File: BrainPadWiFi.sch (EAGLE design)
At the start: 14 parts, among them IC1 ESP-WROOM-02FRONT-FACE, U1 LM3940IMP-3.3/NOPBMP04A-M

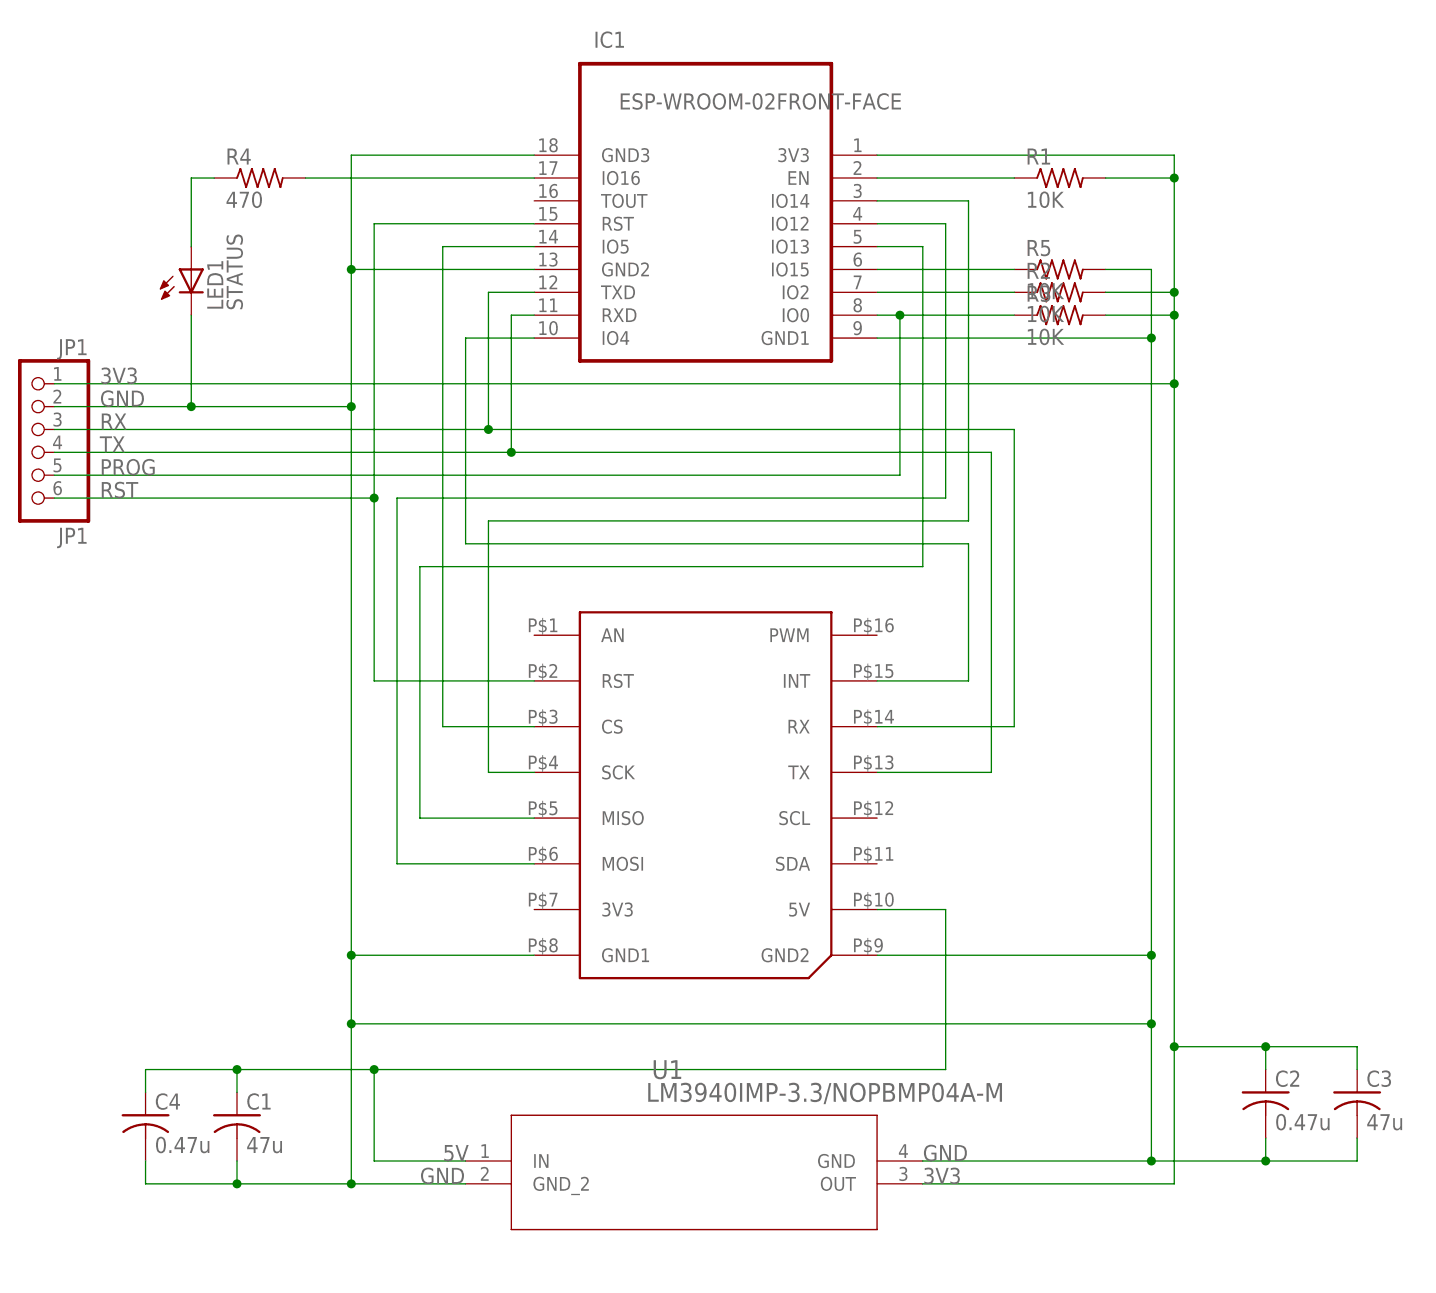
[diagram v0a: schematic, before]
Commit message: Changed regulator.
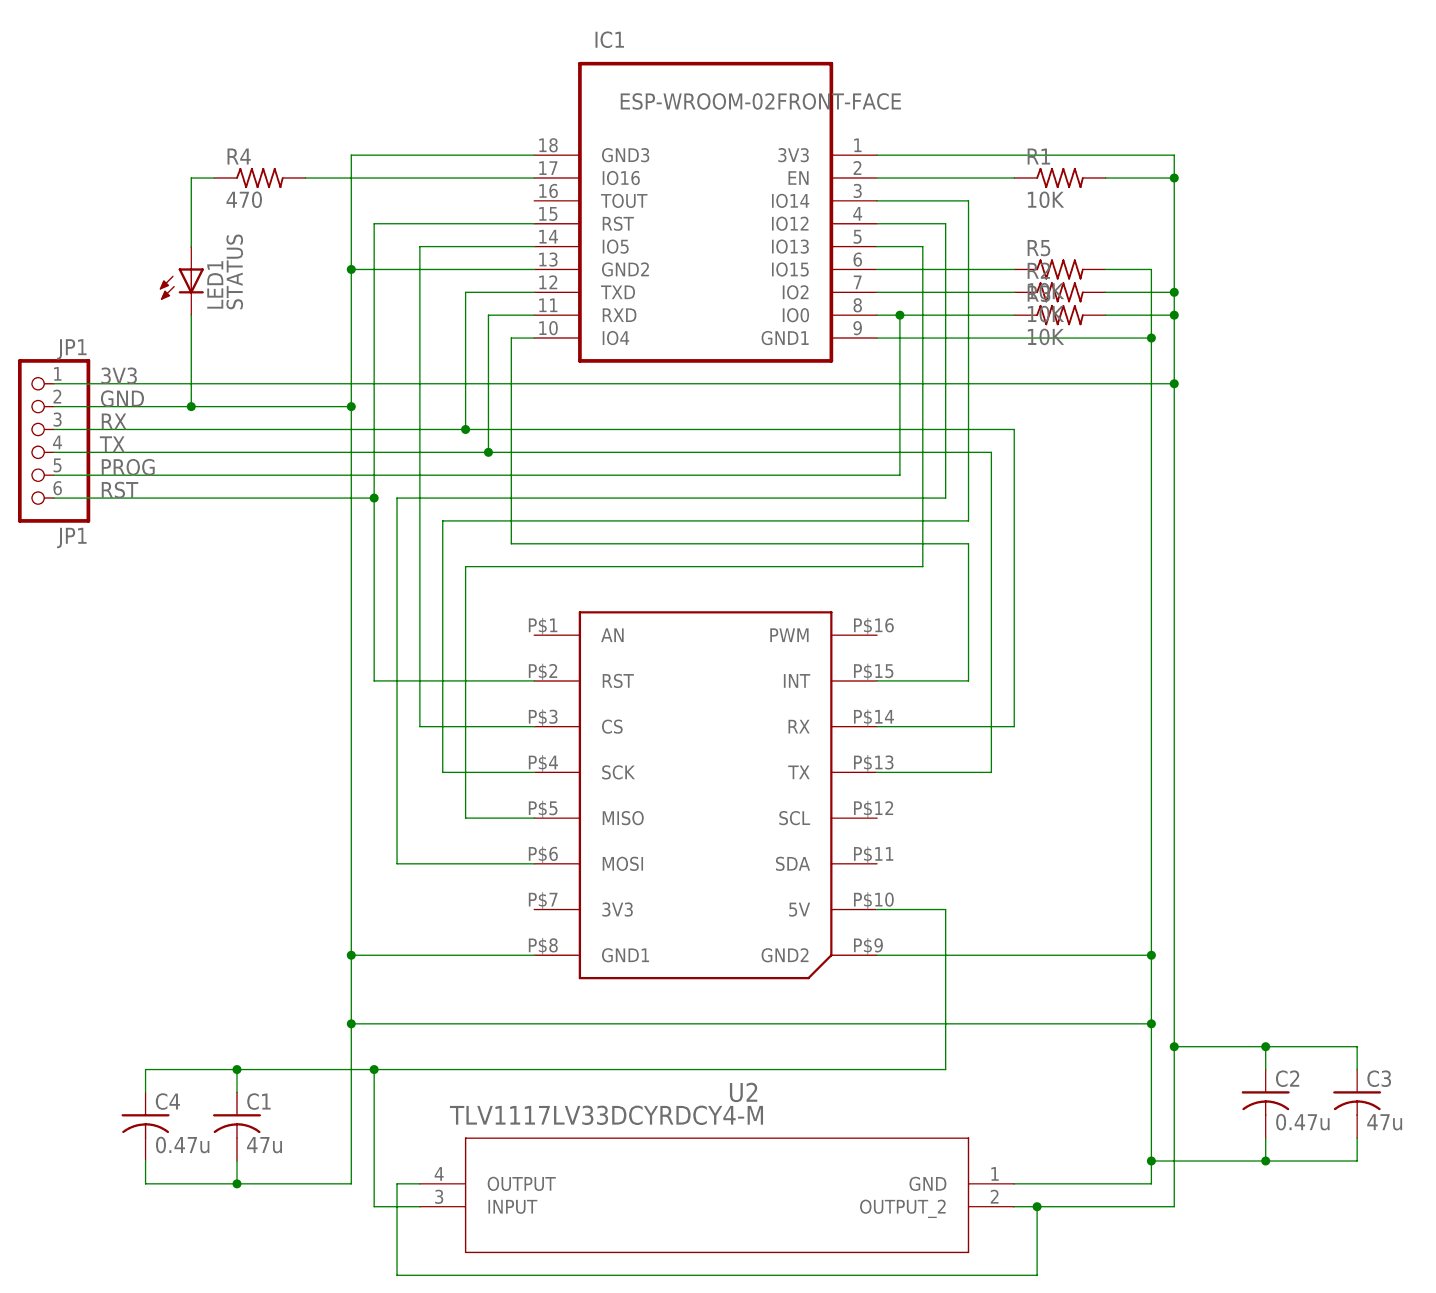
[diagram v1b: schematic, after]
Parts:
- removed U1: LM3940IMP-3.3/NOPBMP04A-M, BrainPadWiFi:LM3940IMP-3.3/NOPBMP04A-M
- added U2: TLV1117LV33DCYRDCY4-M, BrainPadWiFi:TLV1117LV33DCYRDCY4-M
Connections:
- net 3V3: now also U2.OUTPUT, U2.OUTPUT_2; no longer U1.OUT
- net 5V: now also U2.INPUT; no longer U1.IN
- net GND: now also U2.GND; no longer U1.GND, U1.GND_2

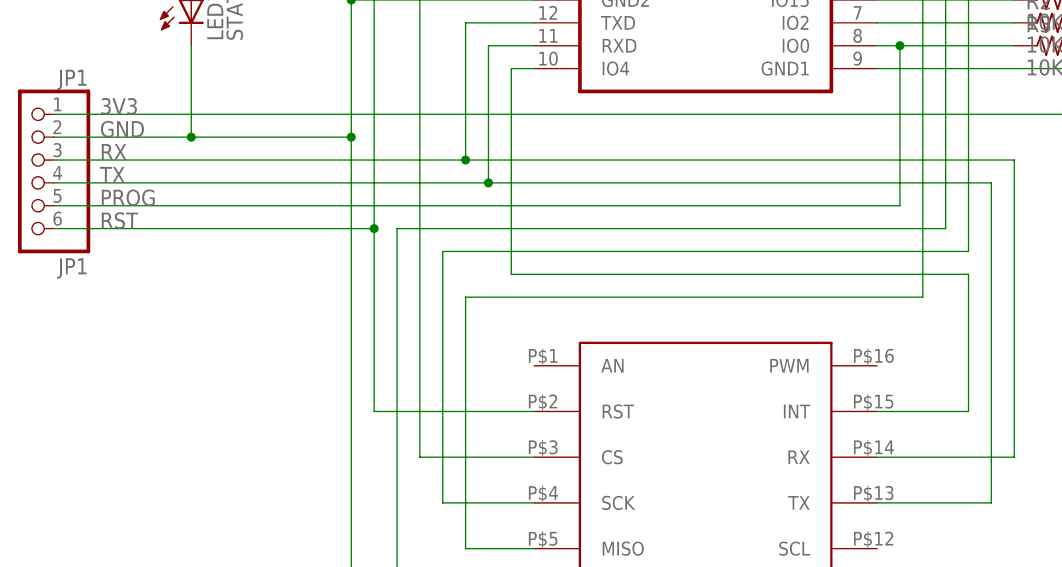
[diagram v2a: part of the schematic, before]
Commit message: PROG line wired because we grant to an ability for self-programming from BrainPad to ESP.
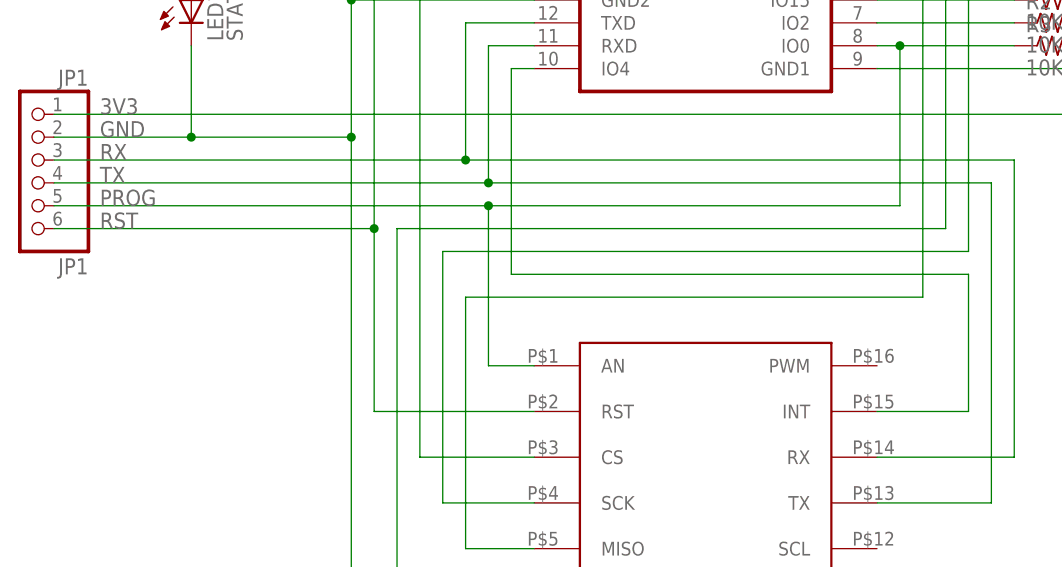
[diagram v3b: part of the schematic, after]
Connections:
- net PROG: now also U$1.AN
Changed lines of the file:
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@@
 <?xml version="1.0" encoding="utf-8"?>
 <!DOCTYPE eagle SYSTEM "eagle.dtd">
-<eagle version="8.7.1">
+<eagle version="9.1.3">
 <drawing>
 <settings>
-<setting alwaysvectorfont="no"/>
+<setting alwaysvectorfont="yes"/>
 <setting verticaltext="up"/>
 </settings>
@@
 <wire x1="101.6" y1="106.68" x2="104.14" y2="106.68" width="0.1524" layer="91"/>
 <wire x1="104.14" y1="106.68" x2="104.14" y2="88.9" width="0.1524" layer="91"/>
-<wire x1="104.14" y1="88.9" x2="10.16" y2="88.9" width="0.1524" layer="91"/>
+<wire x1="104.14" y1="88.9" x2="58.42" y2="88.9" width="0.1524" layer="91"/>
 <pinref part="R3" gate="G$1" pin="1"/>
+<wire x1="58.42" y1="88.9" x2="10.16" y2="88.9" width="0.1524" layer="91"/>
 <wire x1="104.14" y1="106.68" x2="116.84" y2="106.68" width="0.1524" layer="91"/>
 <junction x="104.14" y="106.68"/>
 <label x="15.24" y="88.9" size="1.778" layer="95"/>
 <pinref part="JP1" gate="A" pin="5"/>
-</segment>
-</net>
+<pinref part="U$1" gate="G$1" pin="AN"/>
+<wire x1="58.42" y1="88.9" x2="58.42" y2="71.12" width="0.1524" layer="91"/>
+<wire x1="58.42" y1="71.12" x2="63.5" y2="71.12" width="0.1524" layer="91"/>
+<junction x="58.42" y="88.9"/>
+</segment>
+</net>

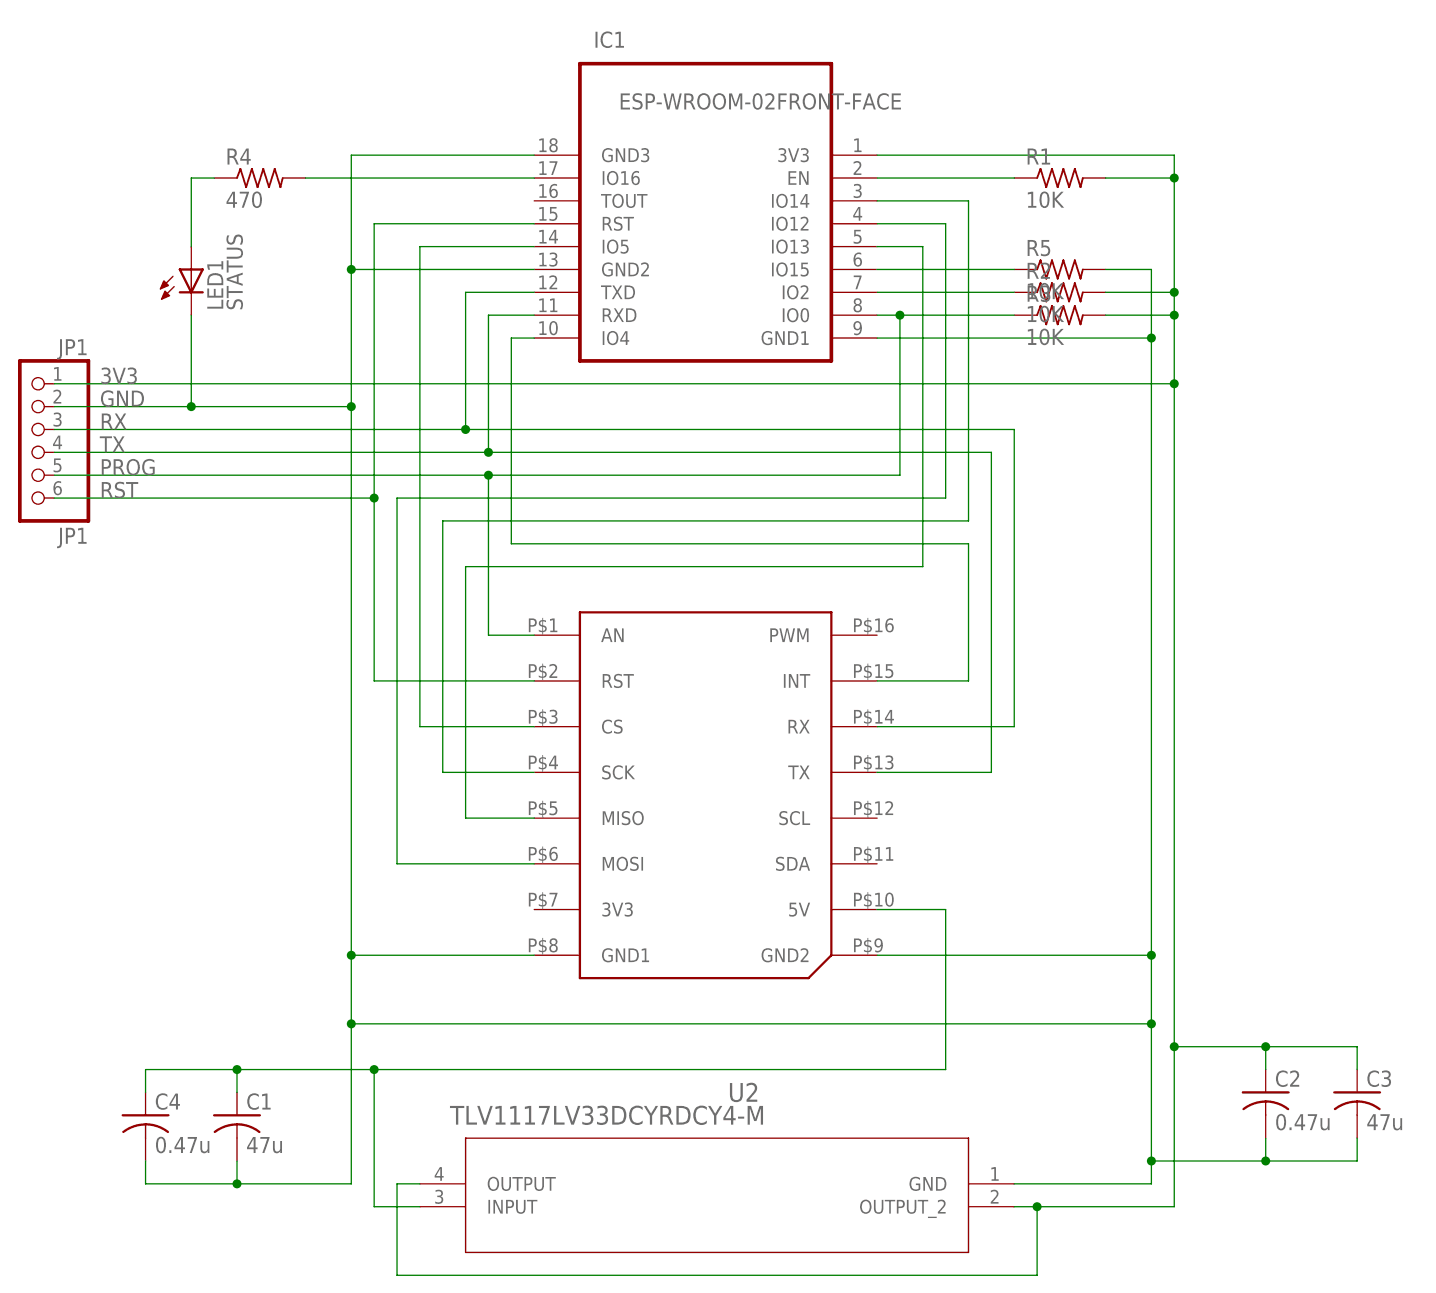
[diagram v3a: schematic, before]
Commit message: Redesigned for next version.
SMT pieces place only front side. (exclude ESP)
Add grove connector.
Registers only 1K.
Add status2 LED.
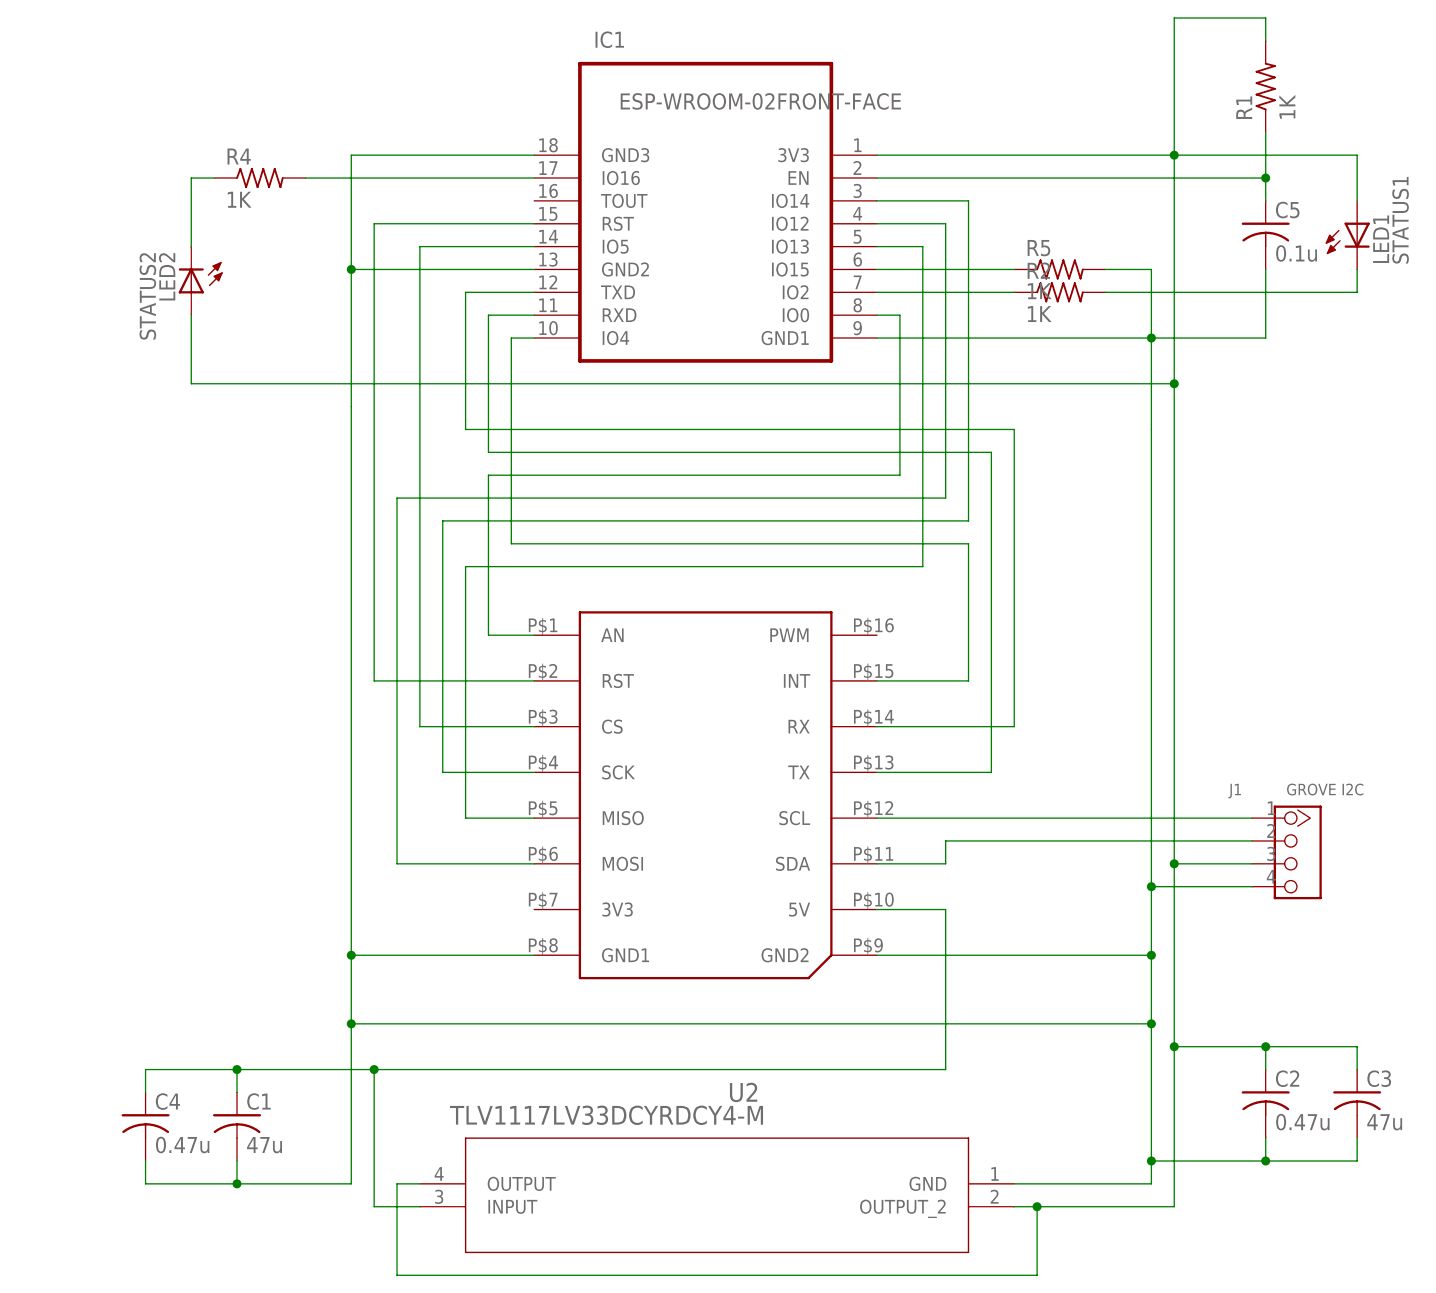
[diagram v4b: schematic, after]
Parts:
- removed JP1: JP1, BrainPadWiFi:PINHD-1X6
- removed R3: 10K, BrainPadWiFi:R-US_R1206
- added C5: 0.1u, BrainPadWiFi:C-USC1206
- added J1: GROVE I2C, BrainPadWiFi:GROVE-CONNECTOR-DIP(4P-2.0)
- added LED2: STATUS2, BrainPadWiFi:LEDSML1206
- LED1: value STATUS -> STATUS1
- R1, R2, R5: value 10K -> 1K
- R4: value 470 -> 1K
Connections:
- net N$1 renamed IO2
- net N$4 renamed IO15
- removed net STAT: LED1.A, R4.1
- new net SCL: J1.1, U$1.SCL
- new net SDA: J1.2, U$1.SDA
- new net STAT1: LED1.C, R2.2
- new net STAT2: LED2.C, R4.1
- net 3V3: now also J1.3, LED1.A, LED2.A; no longer JP1.1, R2.2, R3.2
- net EN: now also C5.1
- net GND: now also C5.2, J1.4; no longer JP1.2, LED1.C
- net PROG: no longer JP1.5, R3.1
- net RST: no longer JP1.6
- net RX: no longer JP1.3
- net TX: no longer JP1.4
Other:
- moved on the sheet: LED1, R1
